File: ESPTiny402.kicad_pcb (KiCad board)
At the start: 2 copper layers, 26.4 x 23.9 mm, 20 parts, among them J1 Conn_01x10_Male, J2 Conn_01x10_Male, J3 Conn_01x04_Male, U1 ESP-01v090, U2 ATtiny402-SS, U3 MCP1700

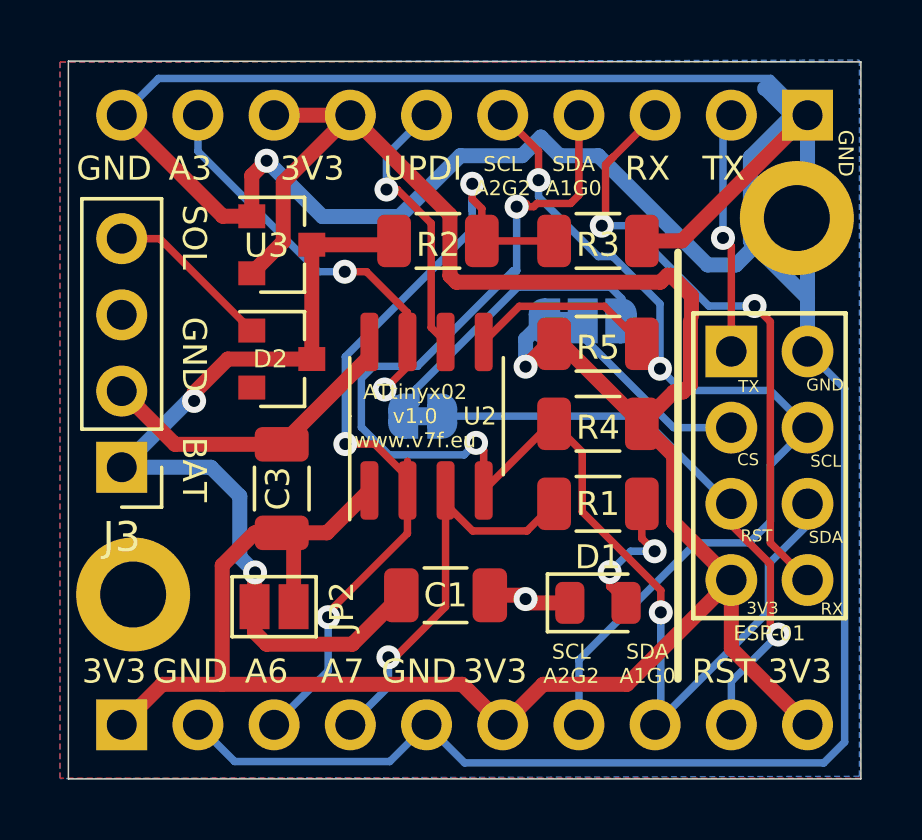
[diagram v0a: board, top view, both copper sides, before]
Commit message: Update 4x2 and README
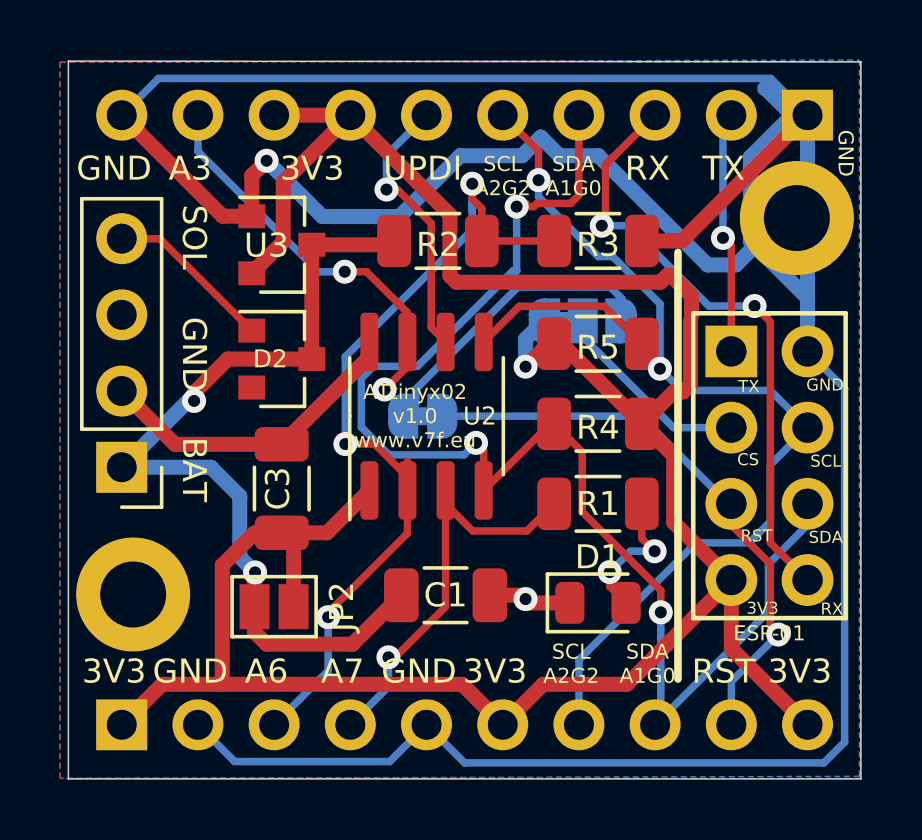
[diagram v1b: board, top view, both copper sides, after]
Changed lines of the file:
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@@
     (descr "Through hole straight pin header, 1x04, 2.54mm pitch, single row")
     (tags "Through hole pin header THT 1x04 2.54mm single row")
-    (fp_text reference J3 (at 0 -2.33) (layer F.SilkS)
+    (fp_text reference J3 (at 0 -2.33) (layer F.SilkS) hide
       (effects (font (size 1 1) (thickness 0.15)))
     )

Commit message: C3 -> C2 rename
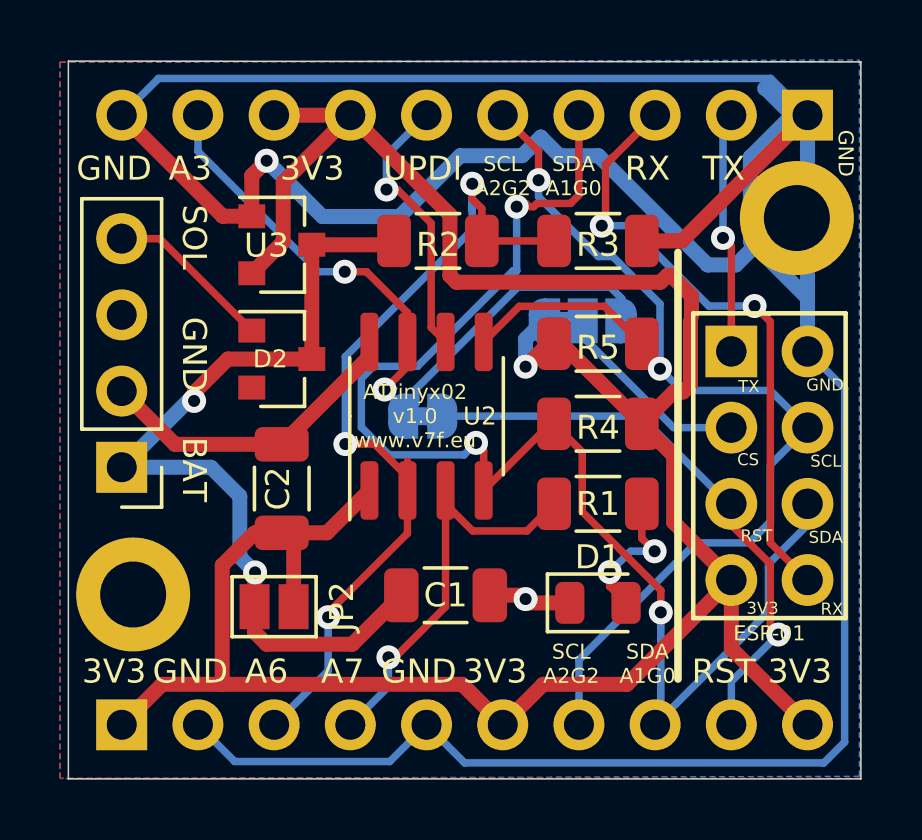
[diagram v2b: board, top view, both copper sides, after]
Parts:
- renumbered C3 to C2
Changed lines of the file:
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@@
     (tags capacitor)
     (attr smd)
-    (fp_text reference C3 (at 0 -0.127 90) (layer F.SilkS)
+    (fp_text reference C2 (at 0 -0.127 90) (layer F.SilkS)
       (effects (font (size 0.8 0.8) (thickness 0.15)))
     )

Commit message: Remove some support 3V3 tracks
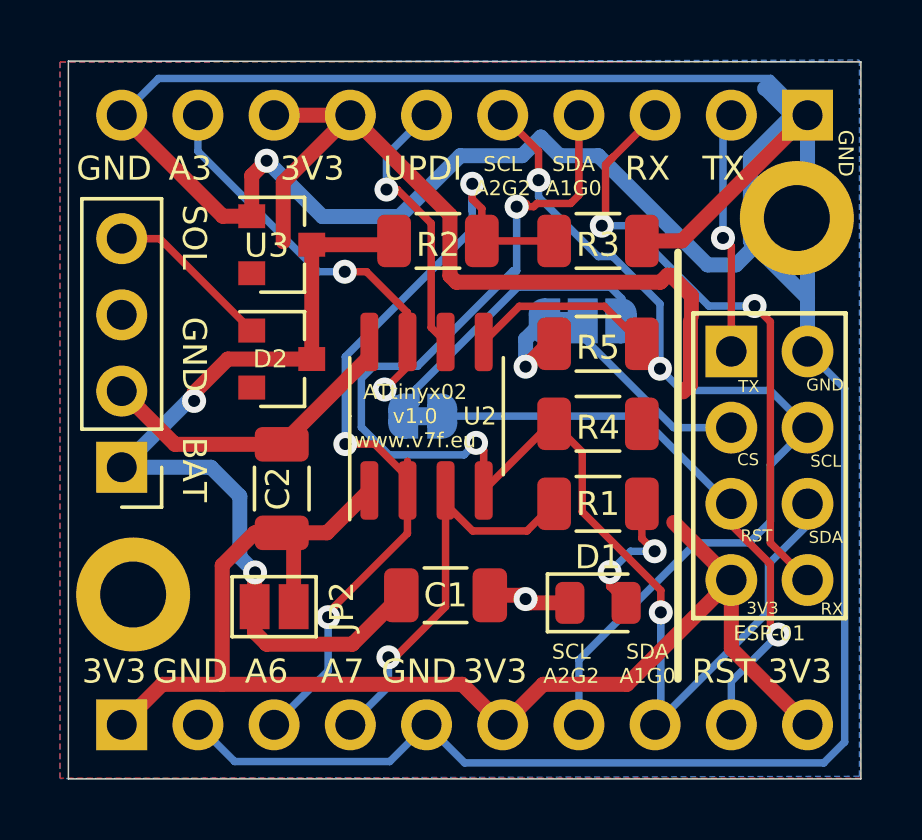
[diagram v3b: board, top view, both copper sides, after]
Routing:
- net +3V3: track 84.7 -> 73.9 mm
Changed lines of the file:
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@@
     (thickness 1.6)
     (drawings 55)
-    (tracks 269)
+    (tracks 263)
     (zones 0)
     (modules 20)
@@
   (layers
     (0 F.Cu signal)
-    (31 B.Cu signal hide)
+    (31 B.Cu signal)
     (32 B.Adhes user)
     (33 F.Adhes user)
@@
   (segment (start 70.358 50.038) (end 71.596601 51.276601) (width 0.25) (layer B.Cu) (net 1) (status 10))
   (segment (start 65.89801 55.73801) (end 67.818 57.658) (width 0.5) (layer F.Cu) (net 2) (status 20))
-  (segment (start 65.89801 53.51351) (end 65.89801 55.73801) (width 0.5) (layer F.Cu) (net 2))
-  (segment (start 64.8355 52.451) (end 65.89801 53.51351) (width 0.5) (layer F.Cu) (net 2) (status 10))
-  (segment (start 62.1685 49.784) (end 64.8355 52.451) (width 0.5) (layer F.Cu) (net 2) (status 30))
   (segment (start 61.9105 49.784) (end 62.1685 49.784) (width 0.5) (layer F.Cu) (net 2) (status 30))
   (segment (start 54.34 56.085) (end 55.753 54.672) (width 0.5) (layer F.Cu) (net 2) (status 20))
@@
   (segment (start 52.578 42.164) (end 55.118 42.164) (width 0.5) (layer F.Cu) (net 2) (status 30))
   (segment (start 52.881999 44.400001) (end 52.881999 46.382001) (width 0.5) (layer F.Cu) (net 2))
-  (segment (start 52.881999 46.382001) (end 51.832 47.432) (width 0.5) (layer F.Cu) (net 2) (status 20))
   (segment (start 55.118 42.164) (end 52.881999 44.400001) (width 0.5) (layer F.Cu) (net 2) (status 10))
   (segment (start 66.454399 51.147601) (end 66.454399 49.022) (width 0.5) (layer F.Cu) (net 2))
   (segment (start 66.21351 51.38849) (end 66.454399 51.147601) (width 0.5) (layer F.Cu) (net 2))
-  (segment (start 65.89801 51.38849) (end 66.21351 51.38849) (width 0.5) (layer F.Cu) (net 2))
-  (segment (start 64.8355 52.451) (end 65.89801 51.38849) (width 0.5) (layer F.Cu) (net 2) (status 10))
   (segment (start 51.932 56.085) (end 50.846999 57.170001) (width 0.5) (layer F.Cu) (net 2) (status 10))
   (segment (start 50.846999 57.170001) (end 50.846999 61.133999) (width 0.5) (layer F.Cu) (net 2))

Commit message: Better power routing
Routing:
- net +3V3: track 73.9 -> 125.0 mm
- net GND: track 132.5 -> 125.0 mm
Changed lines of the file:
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@@
     (thickness 1.6)
     (drawings 55)
-    (tracks 263)
+    (tracks 275)
     (zones 0)
     (modules 20)
@@
   (segment (start 68.961 41.275) (end 68.927002 41.275) (width 0.5) (layer B.Cu) (net 1))
   (segment (start 69.85 42.164) (end 68.961 41.275) (width 0.5) (layer B.Cu) (net 1) (status 10))
-  (segment (start 69.85 42.164) (end 68.453 43.561) (width 0.5) (layer B.Cu) (net 1) (status 10))
   (segment (start 54.187916 45.541898) (end 52.327612 43.681594) (width 0.5) (layer B.Cu) (net 1))
   (segment (start 56.755104 45.541898) (end 54.187916 45.541898) (width 0.5) (layer B.Cu) (net 1))
@@
   (segment (start 70.358 42.164) (end 70.358 45.2374) (width 0.5) (layer B.Cu) (net 1) (status 30))
   (segment (start 70.358 45.9486) (end 70.0024 45.593) (width 0.5) (layer B.Cu) (net 1) (status 30))
-  (segment (start 68.453 46.355) (end 70.358 48.26) (width 0.5) (layer B.Cu) (net 1) (status 10))
-  (segment (start 68.453 43.561) (end 68.453 46.355) (width 0.5) (layer B.Cu) (net 1) (status 20))
   (segment (start 70.358 48.26) (end 70.358 45.9486) (width 0.5) (layer B.Cu) (net 1) (status 20))
   (segment (start 70.358 50.038) (end 70.358 48.26) (width 0.5) (layer B.Cu) (net 1) (status 10))
@@
   (segment (start 71.596601 51.276601) (end 71.596601 63.058401) (width 0.25) (layer B.Cu) (net 1))
   (segment (start 70.358 50.038) (end 71.596601 51.276601) (width 0.25) (layer B.Cu) (net 1) (status 10))
-  (segment (start 65.89801 55.73801) (end 67.818 57.658) (width 0.5) (layer F.Cu) (net 2) (status 20))
   (segment (start 61.9105 49.784) (end 62.1685 49.784) (width 0.5) (layer F.Cu) (net 2) (status 30))
   (segment (start 54.34 56.085) (end 55.753 54.672) (width 0.5) (layer F.Cu) (net 2) (status 20))
@@
   (segment (start 61.548001 61.133999) (end 60.198 62.484) (width 0.5) (layer F.Cu) (net 2) (status 20))
   (segment (start 64.342001 61.133999) (end 61.548001 61.133999) (width 0.5) (layer F.Cu) (net 2))
-  (segment (start 67.818 57.658) (end 64.342001 61.133999) (width 0.5) (layer F.Cu) (net 2) (status 10))
   (segment (start 48.848001 61.133999) (end 47.498 62.484) (width 0.5) (layer F.Cu) (net 2) (status 20))
   (segment (start 60.198 62.484) (end 58.847999 61.133999) (width 0.5) (layer F.Cu) (net 2) (status 10))
@@
   (segment (start 66.454399 51.147601) (end 66.454399 49.022) (width 0.5) (layer F.Cu) (net 2))
   (segment (start 66.21351 51.38849) (end 66.454399 51.147601) (width 0.5) (layer F.Cu) (net 2))
-  (segment (start 51.932 56.085) (end 50.846999 57.170001) (width 0.5) (layer F.Cu) (net 2) (status 10))
-  (segment (start 50.846999 57.170001) (end 50.846999 61.133999) (width 0.5) (layer F.Cu) (net 2))
+  (segment (start 50.846999 56.087001) (end 50.846999 61.133999) (width 0.5) (layer F.Cu) (net 2))
   (segment (start 52.832 56.085) (end 51.932 56.085) (width 0.5) (layer F.Cu) (net 2) (status 30))
   (segment (start 50.846999 61.133999) (end 48.848001 61.133999) (width 0.5) (layer F.Cu) (net 2))
@@
   (segment (start 67.818 59.944) (end 67.818 57.658) (width 0.5) (layer F.Cu) (net 2) (status 20))
   (segment (start 70.358 62.484) (end 67.818 59.944) (width 0.5) (layer F.Cu) (net 2) (status 10))
+  (segment (start 52.832 56.085) (end 50.849 56.085) (width 0.5) (layer F.Cu) (net 2) (status 10))
+  (segment (start 50.849 56.085) (end 50.846999 56.087001) (width 0.5) (layer F.Cu) (net 2))
+  (segment (start 61.423001 63.709001) (end 60.198 62.484) (width 0.25) (layer F.Cu) (net 2) (status 20))
+  (segment (start 69.132999 63.709001) (end 61.423001 63.709001) (width 0.25) (layer F.Cu) (net 2))
+  (segment (start 70.358 62.484) (end 69.132999 63.709001) (width 0.25) (layer F.Cu) (net 2) (status 10))
+  (segment (start 48.723001 63.709001) (end 47.498 62.484) (width 0.25) (layer F.Cu) (net 2) (status 20))
+  (segment (start 58.972999 63.709001) (end 48.723001 63.709001) (width 0.25) (layer F.Cu) (net 2))
+  (segment (start 60.198 62.484) (end 58.972999 63.709001) (width 0.25) (layer F.Cu) (net 2) (status 10))
+  (segment (start 46.909999 40.938999) (end 51.352999 40.938999) (width 0.25) (layer F.Cu) (net 2))
+  (segment (start 46.228 41.620998) (end 46.909999 40.938999) (width 0.25) (layer F.Cu) (net 2))
+  (segment (start 46.228 55.003802) (end 46.228 41.620998) (width 0.25) (layer F.Cu) (net 2))
+  (segment (start 46.347999 55.123801) (end 46.228 55.003802) (width 0.25) (layer F.Cu) (net 2))
+  (segment (start 49.027801 55.123801) (end 46.347999 55.123801) (width 0.25) (layer F.Cu) (net 2))
+  (segment (start 50.154001 56.250001) (end 49.027801 55.123801) (width 0.25) (layer F.Cu) (net 2))
+  (segment (start 50.154001 59.700999) (end 50.154001 56.250001) (width 0.25) (layer F.Cu) (net 2))
+  (segment (start 51.352999 40.938999) (end 52.578 42.164) (width 0.25) (layer F.Cu) (net 2) (status 20))
+  (segment (start 47.498 62.357) (end 50.154001 59.700999) (width 0.25) (layer F.Cu) (net 2) (status 10))
+  (segment (start 47.498 62.484) (end 47.498 62.357) (width 0.25) (layer F.Cu) (net 2) (status 30))
   (via (at 65.260882 56.699306) (size 0.8) (drill 0.4) (layers F.Cu B.Cu) (net 4))
   (segment (start 64.8355 56.273924) (end 65.260882 56.699306) (width 0.25) (layer F.Cu) (net 4))

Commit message: Fix silk screen back
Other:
- board text removed: "TRST UPDI"
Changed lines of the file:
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@@
     )
+  )
+  (gr_text UPDI (at 57.531 43.942) (layer F.SilkS)
+    (effects (font (size 0.8 0.8) (thickness 0.15)))
   )
   (gr_text "ATtinyx02\nv1.0\nwww.v7f.eu" (at 57.277 52.197) (layer F.SilkS)
@@
     (effects (font (size 0.5 0.5) (thickness 0.08)) (justify mirror))
   )
-  (gr_text "TRST\nUPDI" (at 57.404 44.196) (layer B.SilkS)
-    (effects (font (size 0.5 0.5) (thickness 0.1)) (justify mirror))
-  )
   (gr_text 3V3 (at 53.848 44.196) (layer B.SilkS)
     (effects (font (size 0.8 0.8) (thickness 0.15)) (justify mirror))
@@
     (effects (font (size 0.5 0.5) (thickness 0.08)))
   )
-  (gr_text UPDI (at 57.531 43.942) (layer F.SilkS)
-    (effects (font (size 0.8 0.8) (thickness 0.15)))
+  (gr_text UPDI (at 57.531 44.069 180) (layer B.SilkS)
+    (effects (font (size 0.8 0.8) (thickness 0.15)) (justify mirror))
   )
   (gr_text 3V3 (at 53.848 43.942) (layer F.SilkS)
